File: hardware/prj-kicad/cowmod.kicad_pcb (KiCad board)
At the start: 2 copper layers, 146 x 90 mm, 0 parts

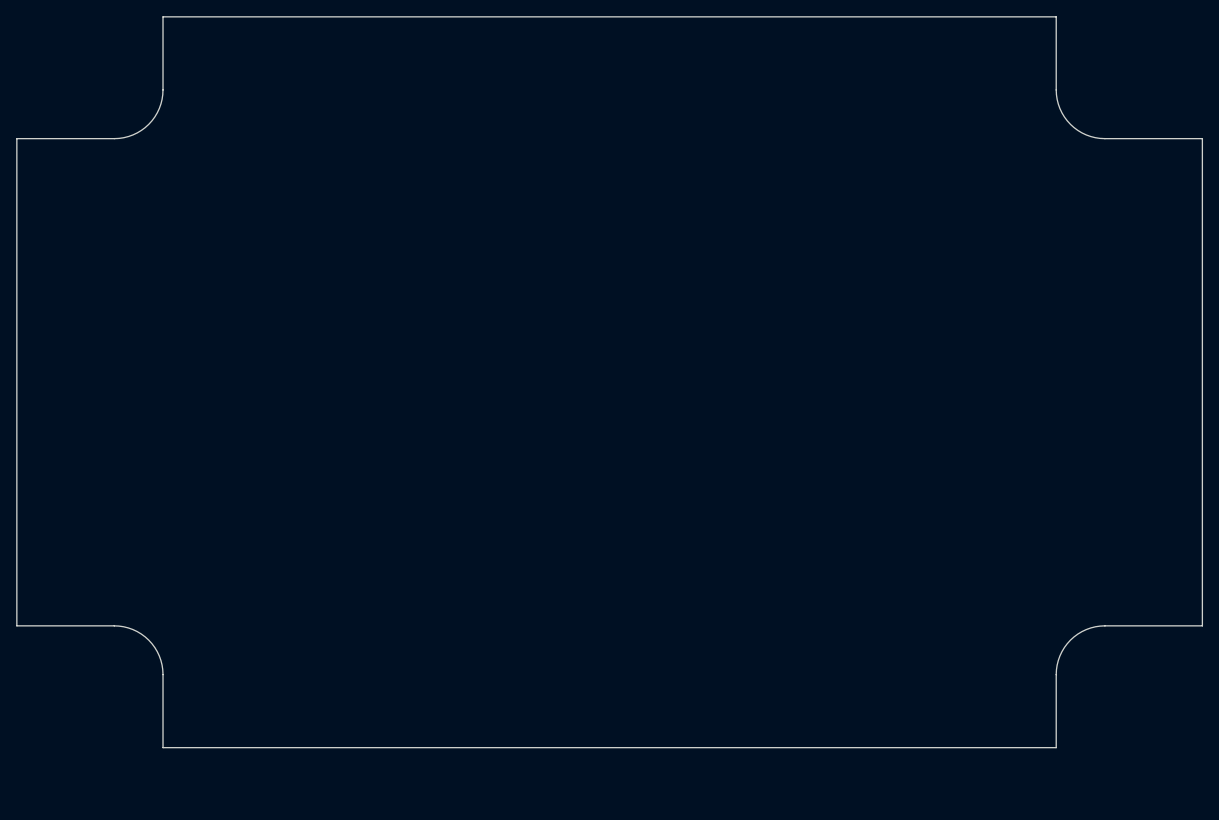
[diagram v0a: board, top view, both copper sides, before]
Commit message: = ADD: Insert FPGA and route all PMOD ports
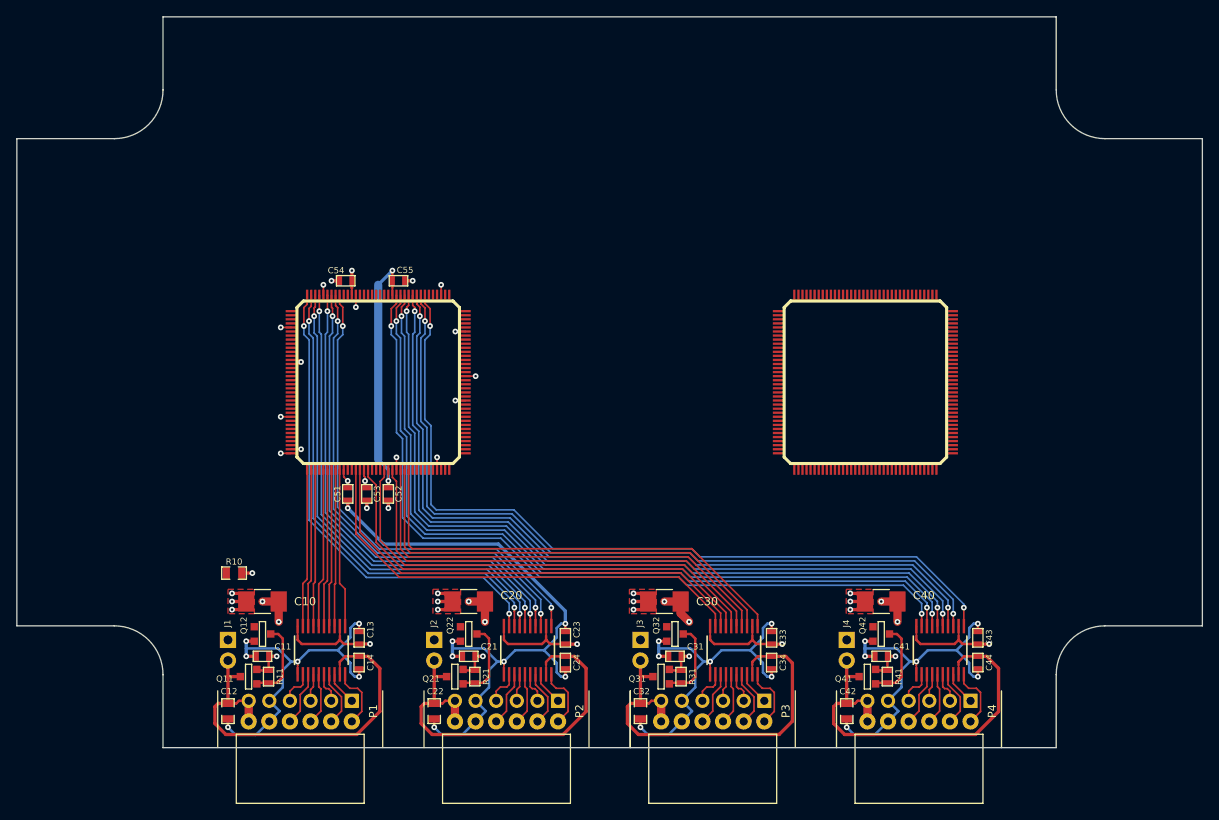
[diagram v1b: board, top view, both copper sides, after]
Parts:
- added C10: 2,2uF, cowmod:SMD1210, F.Cu at (105.8, 132.0)
- added C11: 1uF, cowmod:SMD0603, F.Cu at (105.8, 138.8)
- added C12: 1uF, cowmod:SMD0805, F.Cu at (101.5, 145.5)
- added C13: 100nF, cowmod:SMD0603, F.Cu at (117.7, 136.5)
- added C14: 100nF, cowmod:SMD0603, F.Cu at (117.7, 139.5)
- added C20: 2,2uF, cowmod:SMD1210, F.Cu at (131.2, 132.0)
- added C21: 1uF, cowmod:SMD0603, F.Cu at (131.2, 138.8)
- added C22: 1uF, cowmod:SMD0805, F.Cu at (126.9, 145.5)
- added C23: 100nF, cowmod:SMD0603, F.Cu at (143.1, 136.5)
- added C24: 100nF, cowmod:SMD0603, F.Cu at (143.1, 139.5)
- added C30: 2,2uF, cowmod:SMD1210, F.Cu at (155.2, 132.0)
- added C31: 1uF, cowmod:SMD0603, F.Cu at (156.6, 138.8)
- added C32: 1uF, cowmod:SMD0805, F.Cu at (152.3, 145.5)
- added C33: 100nF, cowmod:SMD0603, F.Cu at (168.4, 136.5)
- added C34: 100nF, cowmod:SMD0603, F.Cu at (168.4, 139.5)
- added C40: 2,2uF, cowmod:SMD1210, F.Cu at (181.9, 132.0)
- added C41: 1uF, cowmod:SMD0603, F.Cu at (181.9, 138.8)
- added C42: 1uF, cowmod:SMD0805, F.Cu at (177.7, 145.5)
- added C43: 100nF, cowmod:SMD0603, F.Cu at (193.8, 136.5)
- added C44: 100nF, cowmod:SMD0603, F.Cu at (193.8, 139.5)
- added C51: 100nF, cowmod:SMD0603, F.Cu at (116.2, 118.8)
- added C52: 100nF, cowmod:SMD0603, F.Cu at (121.2, 118.8)
- added C53: 100nF, cowmod:SMD0603, F.Cu at (118.6, 118.8)
- added C54: 100nF, cowmod:SMD0603, F.Cu at (116.0, 92.5)
- added C55: 100nF, cowmod:SMD0603, F.Cu at (122.5, 92.5)
- added J1: JUMPER, cowmod:CONN_2, F.Cu at (101.5, 138.0)
- added J2: JUMPER, cowmod:CONN_2, F.Cu at (126.9, 138.0)
- added J3: JUMPER, cowmod:CONN_2, F.Cu at (152.3, 138.0)
- added J4: JUMPER, cowmod:CONN_2, F.Cu at (177.7, 138.0)
- added P1: PMOD, cowmod:PMOD_SSW106-RA, F.Cu at (110.4, 145.5)
- added P2: PMOD, cowmod:PMOD_SSW106-RA, F.Cu at (135.8, 145.5)
- added P3: PMOD, cowmod:PMOD_SSW106-RA, F.Cu at (161.2, 145.5)
- added P4: PMOD, cowmod:PMOD_SSW106-RA, F.Cu at (186.6, 145.5)
- added Q11: SI2319C, cowmod:SOT23-3, F.Cu at (104.0, 141.2)
- added Q12: SQ2318, cowmod:SOT23-3, F.Cu at (105.8, 136.0)
- added Q21: SI2319C, cowmod:SOT23-3, F.Cu at (129.4, 141.2)
- added Q22: SQ2318, cowmod:SOT23-3, F.Cu at (131.2, 136.0)
- added Q31: SI2319C, cowmod:SOT23-3, F.Cu at (154.8, 141.2)
- added Q32: SQ2318, cowmod:SOT23-3, F.Cu at (156.6, 136.0)
- added Q41: SI2319C, cowmod:SOT23-3, F.Cu at (180.2, 141.2)
- added Q42: SQ2318, cowmod:SOT23-3, F.Cu at (181.9, 136.0)
- added R10: 0, cowmod:SMD0805, F.Cu at (102.2, 128.5)
- added R11: 100k, cowmod:SMD0603, F.Cu at (106.5, 141.2)
- added R21: 100k, cowmod:SMD0603, F.Cu at (131.9, 141.2)
- added R31: 100k, cowmod:SMD0603, F.Cu at (157.3, 141.2)
- added R41: 100k, cowmod:SMD0603, F.Cu at (182.7, 141.2)
- added TQFP144: VAL**, cowmod:TQFP144, F.Cu at (180.0, 105.0)
- added U11: TXS0108E-PW, cowmod:TSSOP20, F.Cu at (113.0, 138.0)
- added U2: ICE40HX1K-TQ144, cowmod:TQFP144, F.Cu at (120.0, 105.0)
- added U21: TXS0108E-PW, cowmod:TSSOP20, F.Cu at (138.4, 138.0)
- added U31: TXS0108E-PW, cowmod:TSSOP20, F.Cu at (163.8, 138.0)
- added U41: TXS0108E-PW, cowmod:TSSOP20, F.Cu at (189.2, 138.0)
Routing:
- net GND: track 0.00 -> 449.9 mm, vias 0 -> 50
- net +PMOD: track 0.00 -> 334.9 mm, vias 0 -> 21
- net MOD4_IO5: track 0.00 -> 100.0 mm, vias 0 -> 2
- net MOD4_IO1: track 0.00 -> 99.6 mm, vias 0 -> 2
- net MOD4_IO6: track 0.00 -> 99.4 mm, vias 0 -> 2
- net MOD4_IO4: track 0.00 -> 99.3 mm, vias 0 -> 2
- net MOD4_IO8: track 0.00 -> 99.3 mm, vias 0 -> 2
- net MOD4_IO2: track 0.00 -> 99.3 mm, vias 0 -> 2
- net MOD4_IO3: track 0.00 -> 99.2 mm, vias 0 -> 2
- net MOD4_IO7: track 0.00 -> 99.2 mm, vias 0 -> 2
- net +1.2V: track 0.00 -> 61.8 mm, vias 0 -> 5
- net MOD2_IO5: track 0.00 -> 60.5 mm, vias 0 -> 2
- net MOD2_IO1: track 0.00 -> 60.1 mm, vias 0 -> 2
- net MOD2_IO3: track 0.00 -> 59.9 mm, vias 0 -> 2
- net MOD2_IO6: track 0.00 -> 59.9 mm, vias 0 -> 2
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- added copper zone on In1.Cu, net +1.2V
- added copper zone on In1.Cu, net +3.3V
- added copper zone on In1.Cu, net +PMOD
- added copper zone on F.Cu, net GND
- added copper zone on In2.Cu, net GND
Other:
- copper layers 2 -> 4
- net class Default: clearance 0.2 -> 0.1524
- rule trace_clearance: 0.2 -> 0.1524

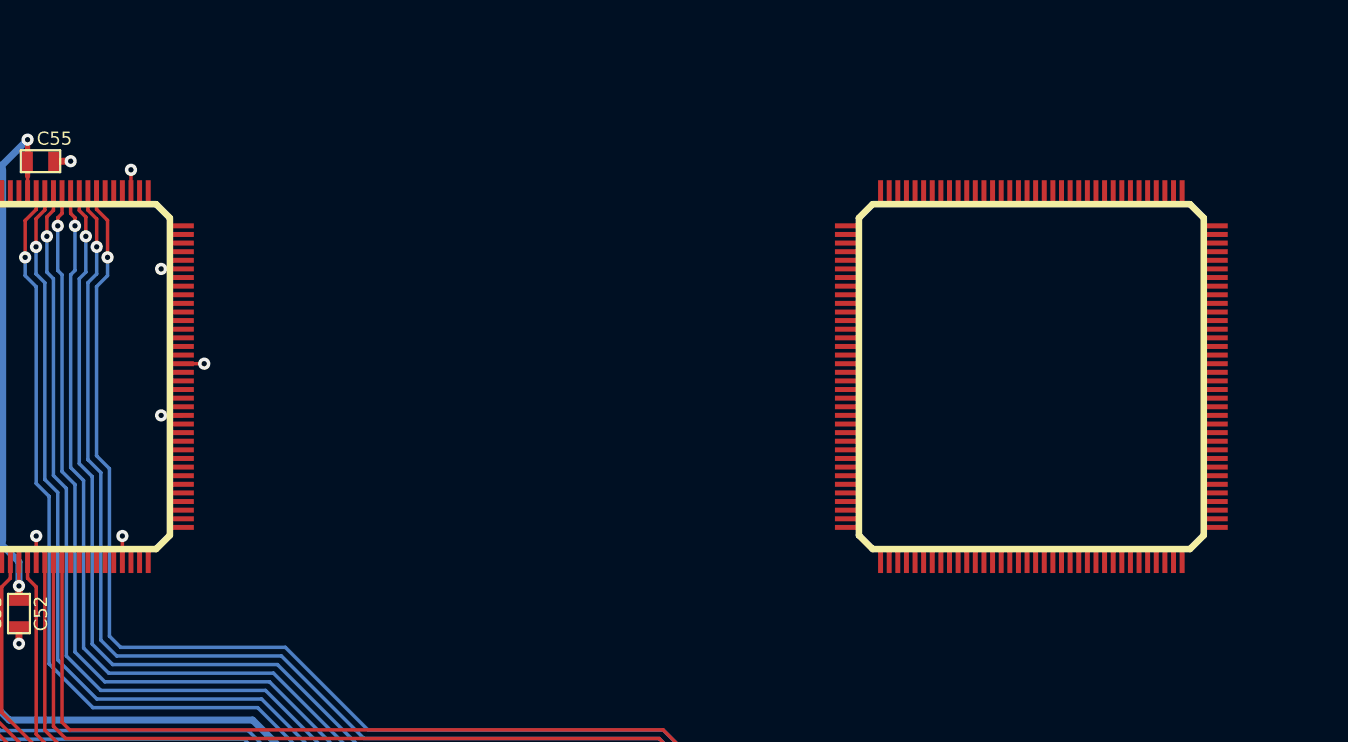
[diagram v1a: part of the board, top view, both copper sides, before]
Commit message: = ADD: Insert main MCU (STM32) and connect it to FPGA
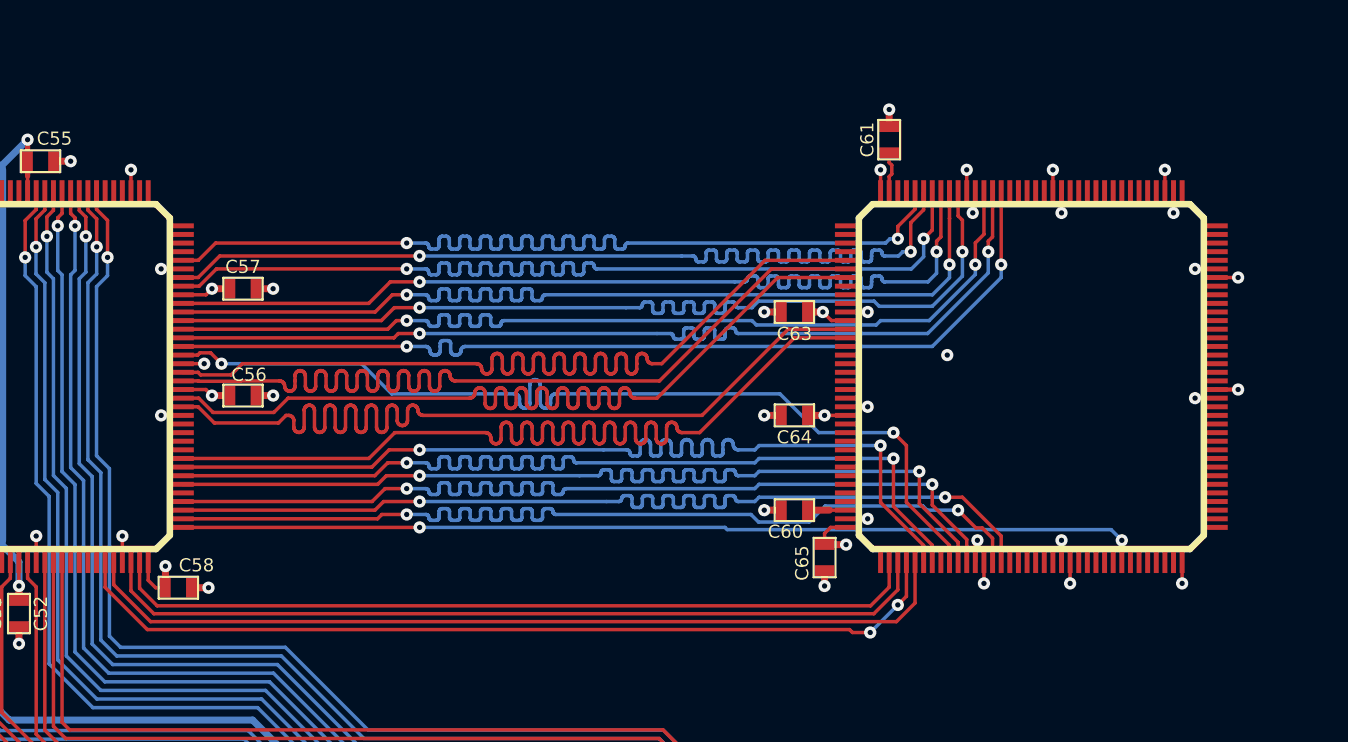
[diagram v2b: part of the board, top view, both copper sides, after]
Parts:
- removed TQFP144: VAL**, cowmod:TQFP144
- added C56: 100nF, cowmod:SMD0603, F.Cu at (134.2, 106.1)
- added C57: 100nF, cowmod:SMD0603, F.Cu at (134.2, 99.9)
- added C58: 100nF, cowmod:SMD0603, F.Cu at (130.5, 117.2)
- added C60: 2,2uF, cowmod:SMD0603, F.Cu at (166.2, 112.8)
- added C61: 2,2uF, cowmod:SMD0603, F.Cu at (171.8, 91.2)
- added C63: 100nF, cowmod:SMD0603, F.Cu at (166.2, 101.2)
- added C64: 100nF, cowmod:SMD0603, F.Cu at (166.2, 107.2)
- added C65: 100nF, cowmod:SMD0603, F.Cu at (168.0, 115.5)
- added U1: STM32F745ZX, cowmod:TQFP144, F.Cu at (180.0, 105.0)
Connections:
- U2 pad 100: Net-(U2-Pad100) -> +3.3V
- U2 pad 101: Net-(U2-Pad101) -> FMC_D10
- U2 pad 102: Net-(U2-Pad102) -> FMC_D11
- U2 pad 104: Net-(U2-Pad104) -> FMC_D12
- U2 pad 67: Net-(U2-Pad67) -> FPGA_MISO
- U2 pad 68: Net-(U2-Pad68) -> FPGA_MOSI
- U2 pad 70: Net-(U2-Pad70) -> FPGA_SCK
- U2 pad 71: Net-(U2-Pad71) -> FPGA_NSS
- U2 pad 73: Net-(U2-Pad73) -> FMC_NADV
- U2 pad 74: Net-(U2-Pad74) -> FMC_NWAIT
- U2 pad 75: Net-(U2-Pad75) -> FMC_NE1
- U2 pad 76: Net-(U2-Pad76) -> FMC_NWE
- U2 pad 78: Net-(U2-Pad78) -> FMC_NOE
- U2 pad 79: Net-(U2-Pad79) -> FMC_D3
- U2 pad 80: Net-(U2-Pad80) -> FMC_D2
- U2 pad 81: Net-(U2-Pad81) -> FMC_D1
- U2 pad 87: Net-(U2-Pad87) -> FMC_D0
- U2 pad 88: Net-(U2-Pad88) -> FMC_D15
- U2 pad 89: Net-(U2-Pad89) -> +3.3V
- U2 pad 90: Net-(U2-Pad90) -> FMC_D14
- U2 pad 91: Net-(U2-Pad91) -> FMC_D13
- U2 pad 93: Net-(U2-Pad93) -> FMC_CLK
- U2 pad 94: Net-(U2-Pad94) -> FMC_D4
- U2 pad 95: Net-(U2-Pad95) -> FMC_D5
- U2 pad 96: Net-(U2-Pad96) -> FMC_D6
- U2 pad 97: Net-(U2-Pad97) -> FMC_D7
- U2 pad 98: Net-(U2-Pad98) -> FMC_D8
- U2 pad 99: Net-(U2-Pad99) -> FMC_D9
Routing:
- net GND: track 449.9 -> 639.4 mm, vias 50 -> 68
- net +3.3V: track 0.00 -> 159.3 mm, vias 0 -> 15
- net FMC_D1: track 0.00 -> 59.0 mm
- net FMC_D11: track 0.00 -> 56.1 mm, vias 0 -> 2
- net FMC_D7: track 0.00 -> 56.1 mm, vias 0 -> 2
- net FMC_D10: track 0.00 -> 56.1 mm, vias 0 -> 2
- net FMC_D9: track 0.00 -> 56.1 mm, vias 0 -> 2
- net FMC_D5: track 0.00 -> 56.1 mm, vias 0 -> 2
- net FMC_NADV: track 0.00 -> 56.1 mm, vias 0 -> 2
- net FMC_D6: track 0.00 -> 56.1 mm, vias 0 -> 2
- net FMC_NWAIT: track 0.00 -> 56.1 mm, vias 0 -> 2
- net FMC_NOE: track 0.00 -> 56.1 mm, vias 0 -> 2
- net FMC_NWE: track 0.00 -> 56.1 mm, vias 0 -> 2
- net FMC_D8: track 0.00 -> 56.1 mm, vias 0 -> 2
- net FMC_D12: track 0.00 -> 56.0 mm, vias 0 -> 2
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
